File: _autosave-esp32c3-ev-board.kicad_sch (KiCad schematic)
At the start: 66 parts, among them IC1 SPX3819M5-L-3-3, IC2 ACS711EEXTK-31AB-T, IC3 ESP32-C3FH4, IC4 W25Q128JVSIQ, J1 Battery Neg(Series), J2 Battery Pos, J3 Barrel_Jack, J4 Conn_01x04_Pin, J5 USB_C_Receptacle_USB2.0, SW1 SW_DPST_x2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

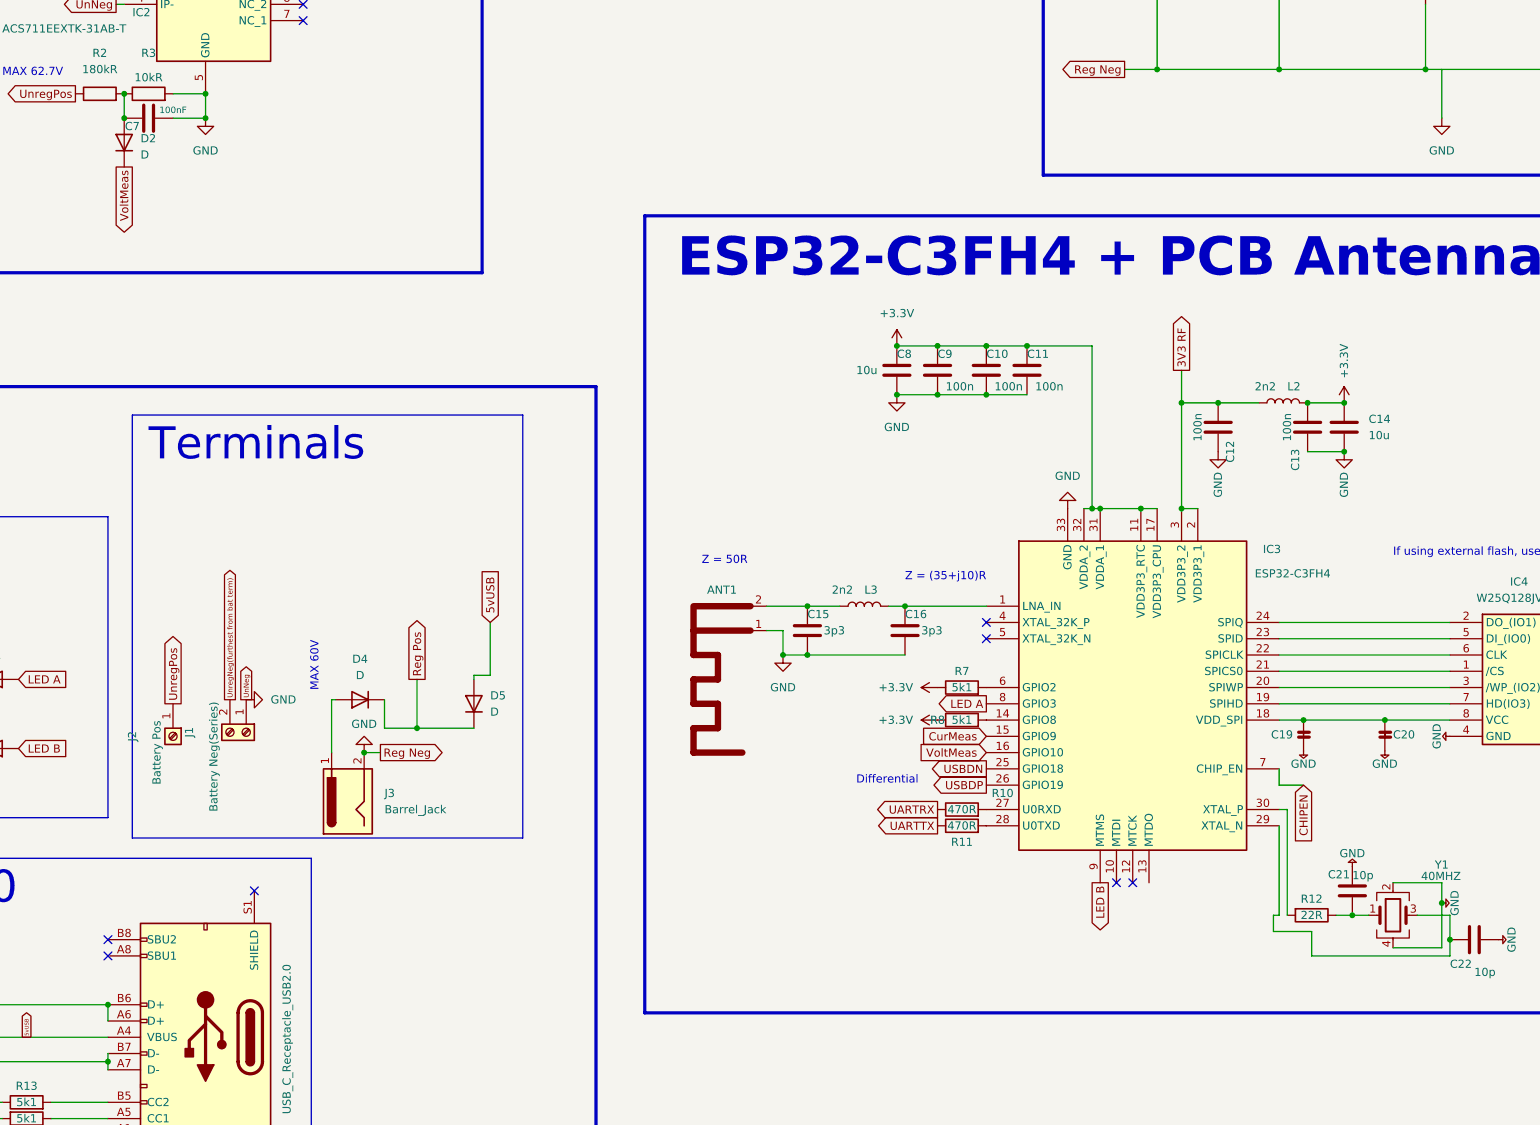
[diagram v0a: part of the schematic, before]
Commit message: almost completed board layout
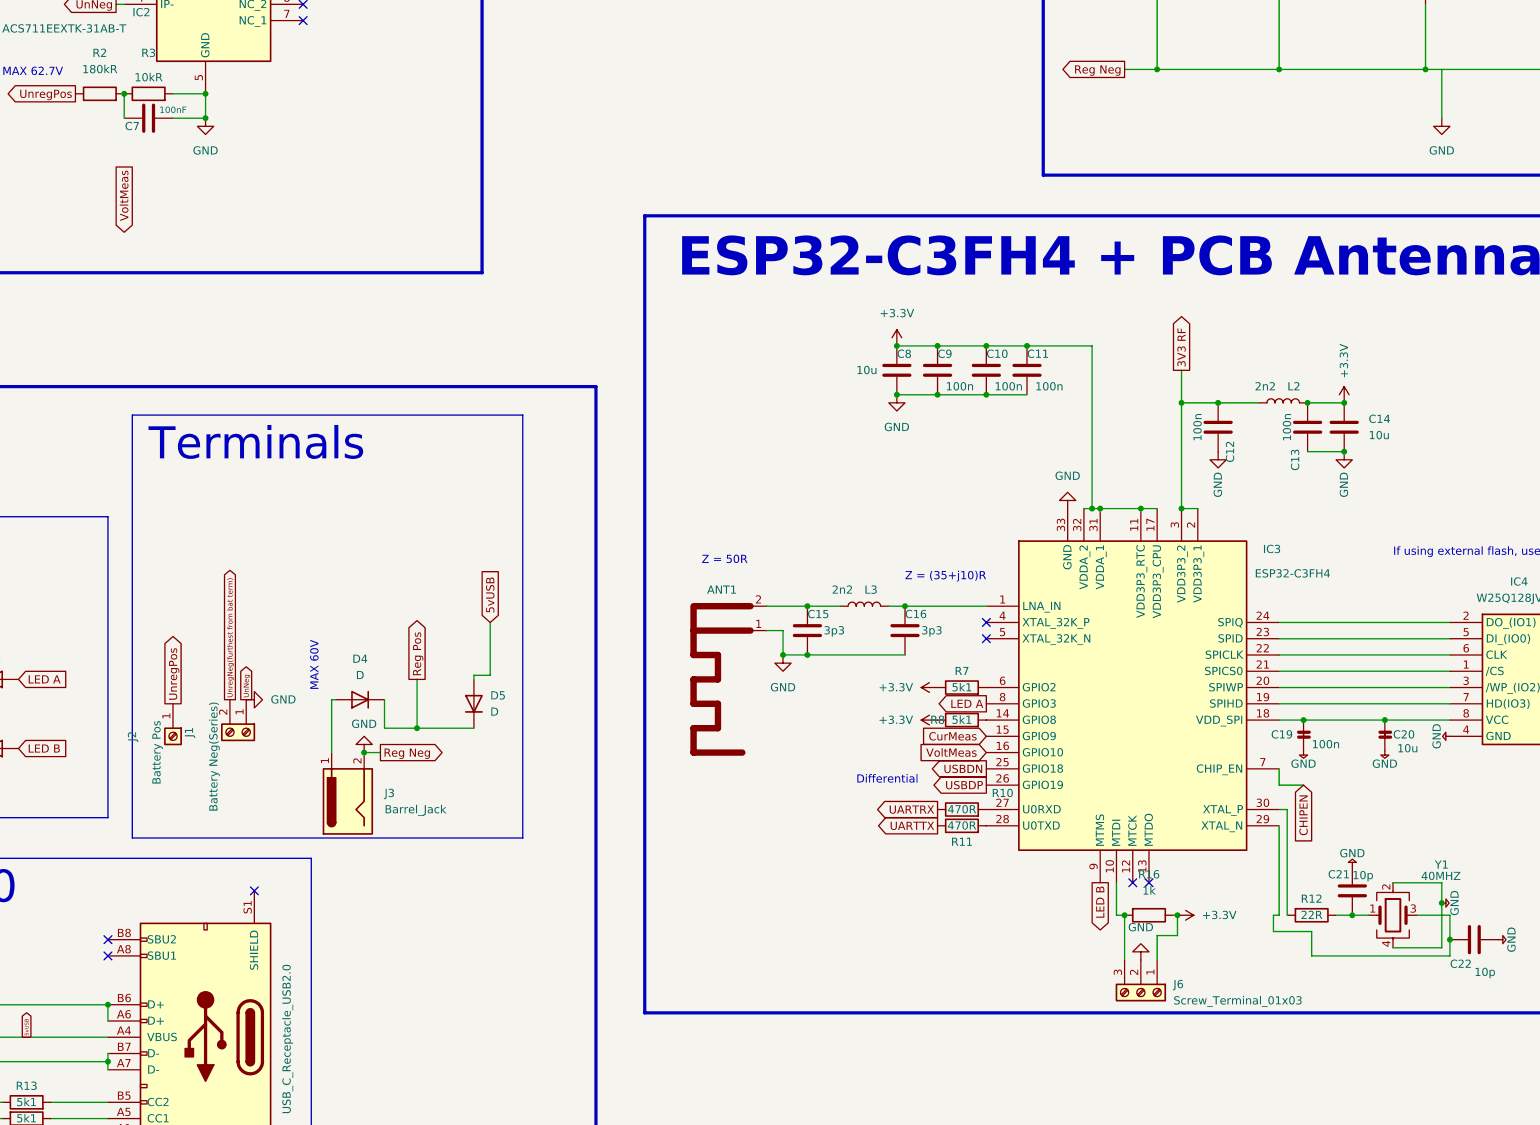
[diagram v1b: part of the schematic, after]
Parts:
- removed D2: D, Diode_SMD:D_SMB_Handsoldering, symbol Device:D
- added J6: Screw_Terminal_01x03, Connector_PinSocket_2.54mm:PinSocket_1x03_P2.54mm_Vertical, symbol Connector:Screw_Terminal_01x03
- added R16: 1k, Resistor_SMD:R_0805_2012Metric_Pad1.20x1.40mm_HandSolder, symbol Device:R
- C19: value C -> 100n
- C20: value C -> 10u
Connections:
- net +3.3V: now also J6.1 (Pin_1), R16.1
- net GND: now also J6.2 (Pin_2)
- net at IC3.10 (MTDI): now also J6.3 (Pin_3), R16.2
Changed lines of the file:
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@@
   (junction (at 151.13 254) (diameter 0) (color 0 0 0 0)
   )
-  (junction (at 153.67 106.68) (diameter 0) (color 0 0 0 0)
-  )
   (junction (at 334.01 76.2) (diameter 0) (color 0 0 0 0)
   )
+  (junction (at 318.135 231.14) (diameter 0) (color 0 0 0 0)
+  )
   (junction (at 151.13 245.11) (diameter 0) (color 0 0 0 0)
   )
@@
   )
   (junction (at 132.08 265.43) (diameter 0) (color 0 0 0 0)
+  )
+  (junction (at 309.88 231.14) (diameter 0) (color 0 0 0 0)
   )
   (junction (at 314.96 83.82) (diameter 0) (color 0 0 0 0)
@@
   (no_connect (at 181.61 86.36))
   (no_connect (at 151.13 237.49))
+  (no_connect (at 313.69 226.06))
   (no_connect (at 288.29 187.96))
   (no_connect (at 181.61 88.9))
   (no_connect (at 173.99 227.33))
   (no_connect (at 151.13 234.95))
-  (no_connect (at 308.61 226.06))
   (no_connect (at 288.29 185.42))
   (no_connect (at 181.61 83.82))
@@
     (stroke (width 0) (type default))
   )
+  (wire (pts (xy 314.96 234.315) (xy 318.135 234.315))
+    (stroke (width 0) (type default))
+  )
   (wire (pts (xy 334.01 231.14) (xy 334.01 217.17))
     (stroke (width 0) (type default))
@@
     (stroke (width 0) (type default))
   )
+  (wire (pts (xy 314.96 238.125) (xy 314.96 234.315))
+    (stroke (width 0) (type default))
+  )
   (wire (pts (xy 360.68 231.14) (xy 360.68 234.95))
     (stroke (width 0) (type default))
@@
     (stroke (width 0) (type default))
   )
+  (wire (pts (xy 317.5 231.14) (xy 318.135 231.14))
+    (stroke (width 0) (type default))
+  )
   (wire (pts (xy 152.4 88.9) (xy 153.67 88.9))
     (stroke (width 0) (type default))
   )
+  (wire (pts (xy 308.61 231.14) (xy 308.61 226.06))
+    (stroke (width 0) (type default))
+  )
   (wire (pts (xy 166.37 66.04) (xy 166.37 68.58))
     (stroke (width 0) (type default))
@@
     (stroke (width 0) (type default))
   )
+  (wire (pts (xy 309.88 238.125) (xy 309.88 231.14))
+    (stroke (width 0) (type default))
+  )
   (wire (pts (xy 334.01 190.5) (xy 360.68 190.5))
     (stroke (width 0) (type default))
@@
     (stroke (width 0) (type default))
   )
+  (wire (pts (xy 309.88 231.14) (xy 308.61 231.14))
+    (stroke (width 0) (type default))
+  )
   (wire (pts (xy 157.48 66.04) (xy 166.37 66.04))
     (stroke (width 0) (type default))
@@
   )
   (wire (pts (xy 162.56 71.12) (xy 163.83 71.12))
+    (stroke (width 0) (type default))
+  )
+  (wire (pts (xy 318.135 234.315) (xy 318.135 231.14))
     (stroke (width 0) (type default))
   )
@@
     )
   )
-  (symbol (lib_id "Device:D") (at 153.67 110.49 90) (unit 1)
-    (in_bom yes) (on_board yes) (dnp no)
-    (property "Reference" "D2" (at 156.21 109.855 90)
-      (effects (font (size 1.27 1.27)) (justify right))
-    )
-    (property "Value" "D" (at 156.21 112.395 90)
-      (effects (font (size 1.27 1.27)) (justify right))
-    )
-    (property "Footprint" "Diode_SMD:D_SMB_Handsoldering" (at 153.67 110.49 0)
-      (effects (font (size 1.27 1.27)) hide)
-    )
-    (property "Datasheet" "~" (at 153.67 110.49 0)
-      (effects (font (size 1.27 1.27)) hide)
-    )
-    (property "Sim.Device" "D" (at 153.67 110.49 0)
-      (effects (font (size 1.27 1.27)) hide)
-    )
-    (property "Sim.Pins" "1=K 2=A" (at 153.67 110.49 0)
-      (effects (font (size 1.27 1.27)) hide)
-    )
-    (pin "1")
-    (pin "2")
-    (instances
-      (project "esp32c3-ev-board"
-        (path "/f5da1fcc-93b5-4c63-bb34-c18c11bc243c"
-          (reference "D2") (unit 1)
-        )
-      )
-    )
-  )
   (symbol (lib_id "Power_Protection:USBLC6-2SC6") (at 121.92 250.19 270) (unit 1)
     (in_bom yes) (on_board yes) (dnp no)
@@
     )
   )
+  (symbol (lib_id "power:GND") (at 312.42 238.125 180) (unit 1)
+    (in_bom yes) (on_board yes) (dnp no) (fields_autoplaced)
+    (property "Reference" "#PWR037" (at 312.42 231.775 0)
+      (effects (font (size 1.27 1.27)) hide)
+    )
+    (property "Value" "GND" (at 312.42 233.045 0)
+      (effects (font (size 1.27 1.27)))
+    )
+    (property "Footprint" "" (at 312.42 238.125 0)
+      (effects (font (size 1.27 1.27)) hide)
+    )
+    (property "Datasheet" "" (at 312.42 238.125 0)
+      (effects (font (size 1.27 1.27)) hide)
+    )
+    (pin "1")
+    (instances
+      (project "esp32c3-ev-board"
+        (path "/f5da1fcc-93b5-4c63-bb34-c18c11bc243c"
+          (reference "#PWR037") (unit 1)
+        )
+      )
+    )
+  )
   (symbol (lib_id "power:+3.3V") (at 55.88 184.15 0) (unit 1)
     (in_bom yes) (on_board yes) (dnp no) (fields_autoplaced)
@@
         (path "/f5da1fcc-93b5-4c63-bb34-c18c11bc243c"
           (reference "J1") (unit 1)
+        )
+      )
+    )
+  )
+  (symbol (lib_id "Device:R") (at 313.69 231.14 270) (unit 1)
+    (in_bom yes) (on_board yes) (dnp no) (fields_autoplaced)
+    (property "Reference" "R16" (at 313.69 224.79 90)
+      (effects (font (size 1.27 1.27)))
+    )
+    (property "Value" "1k" (at 313.69 227.33 90)
+      (effects (font (size 1.27 1.27)))
+    )
+    (property "Footprint" "Resistor_SMD:R_0805_2012Metric_Pad1.20x1.40mm_HandSolder" (at 313.69 229.362 90)
+      (effects (font (size 1.27 1.27)) hide)
+    )
+    (property "Datasheet" "~" (at 313.69 231.14 0)
+      (effects (font (size 1.27 1.27)) hide)
+    )
+    (pin "1")
+    (pin "2")
+    (instances
+      (project "esp32c3-ev-board"
+        (path "/f5da1fcc-93b5-4c63-bb34-c18c11bc243c"
+          (reference "R16") (unit 1)
         )
       )
@@
     )
   )
+  (symbol (lib_id "Connector:Screw_Terminal_01x03") (at 312.42 243.205 270) (unit 1)
+    (in_bom yes) (on_board yes) (dnp no) (fields_autoplaced)
+    (property "Reference" "J6" (at 317.5 241.935 90)
+      (effects (font (size 1.27 1.27)) (justify left))
+    )
+    (property "Value" "Screw_Terminal_01x03" (at 317.5 244.475 90)
+      (effects (font (size 1.27 1.27)) (justify left))
+    )
+    (property "Footprint" "Connector_PinSocket_2.54mm:PinSocket_1x03_P2.54mm_Vertical" (at 312.42 243.205 0)
+      (effects (font (size 1.27 1.27)) hide)
+    )
+    (property "Datasheet" "~" (at 312.42 243.205 0)
+      (effects (font (size 1.27 1.27)) hide)
+    )
+    (pin "1")
+    (pin "2")
+    (pin "3")
+    (instances
+      (project "esp32c3-ev-board"
+        (path "/f5da1fcc-93b5-4c63-bb34-c18c11bc243c"
+          (reference "J6") (unit 1)
+        )
+      )
+    )
+  )
   (symbol (lib_name "+3.3V_1") (lib_id "power:+3.3V") (at 382.27 76.2 0) (unit 1)
     (in_bom yes) (on_board yes) (dnp no) (fields_autoplaced)
@@
         (path "/f5da1fcc-93b5-4c63-bb34-c18c11bc243c"
           (reference "C22") (unit 1)
+        )
+      )
+    )
+  )
+  (symbol (lib_id "power:+3.3V") (at 318.135 231.14 270) (unit 1)
+    (in_bom yes) (on_board yes) (dnp no) (fields_autoplaced)
+    (property "Reference" "#PWR038" (at 314.325 231.14 0)
+      (effects (font (size 1.27 1.27)) hide)
+    )
+    (property "Value" "+3.3V" (at 321.945 231.14 90)
+      (effects (font (size 1.27 1.27)) (justify left))
+    )
+    (property "Footprint" "" (at 318.135 231.14 0)
+      (effects (font (size 1.27 1.27)) hide)
+    )
+    (property "Datasheet" "" (at 318.135 231.14 0)
+      (effects (font (size 1.27 1.27)) hide)
+    )
+    (pin "1")
+    (instances
+      (project "esp32c3-ev-board"
+        (path "/f5da1fcc-93b5-4c63-bb34-c18c11bc243c"
+          (reference "#PWR038") (unit 1)
         )
       )
@@
       (effects (font (size 1.27 1.27)) (justify left))
     )
-    (property "Value" "C" (at 341.63 204.216 0)
-      (effects (font (size 1.27 1.27)) (justify left) hide)
+    (property "Value" "100n" (at 339.09 204.47 0)
+      (effects (font (size 1.27 1.27)) (justify left))
     )
     (property "Footprint" "Capacitor_SMD:C_0603_1608Metric_Pad1.08x0.95mm_HandSolder" (at 338.7852 206.756 0)
@@
       (effects (font (size 1.27 1.27)) (justify left))
     )
-    (property "Value" "C" (at 354.33 204.216 0)
-      (effects (font (size 1.27 1.27)) (justify left) hide)
+    (property "Value" "10u" (at 352.425 205.105 0)
+      (effects (font (size 1.27 1.27)) (justify left))
     )
     (property "Footprint" "Capacitor_SMD:C_0603_1608Metric_Pad1.08x0.95mm_HandSolder" (at 351.4852 206.756 0)
